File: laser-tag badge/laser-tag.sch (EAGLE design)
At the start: 32 parts, among them U1 MKL27Z256VLH4

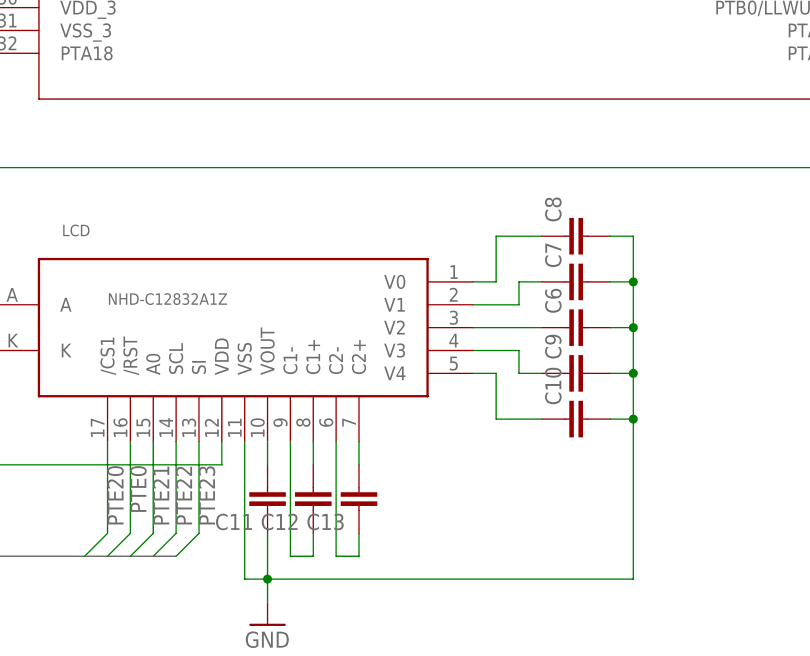
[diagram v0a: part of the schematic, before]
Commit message: Add LCD capacitor values
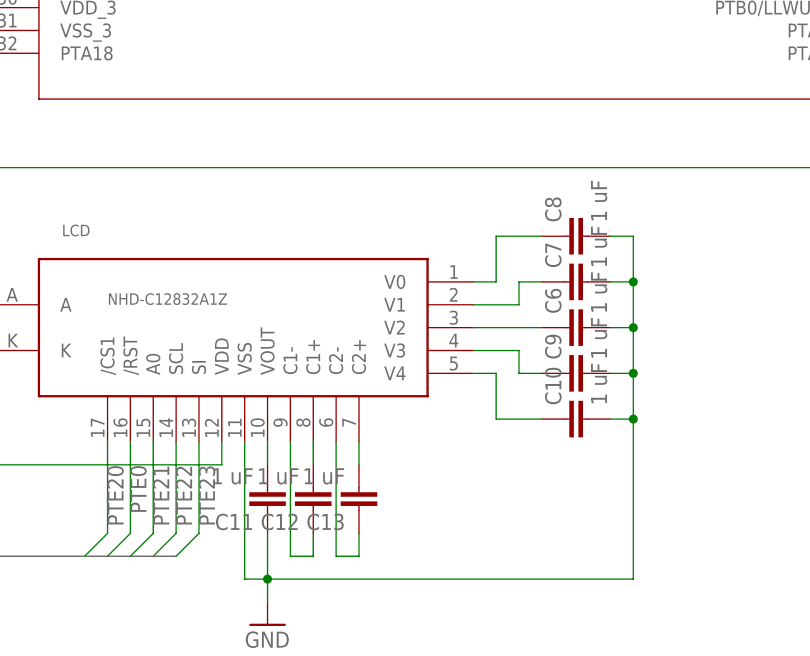
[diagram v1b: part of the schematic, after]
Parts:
- C10, C11, C12, C13, C6, C7, C8, C9: value (none) -> 1 uF
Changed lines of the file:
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@@
 <part name="P+5" library="supply1" deviceset="VCC" device=""/>
 <part name="LCD" library="Displays" deviceset="NHD-C12832A1Z" device=""/>
-<part name="C6" library="rcl" deviceset="C-EU" device="C0603K"/>
-<part name="C7" library="rcl" deviceset="C-EU" device="C0603K"/>
-<part name="C8" library="rcl" deviceset="C-EU" device="C0603K"/>
-<part name="C9" library="rcl" deviceset="C-EU" device="C0603K"/>
-<part name="C10" library="rcl" deviceset="C-EU" device="C0603K"/>
-<part name="C11" library="rcl" deviceset="C-EU" device="C0603K"/>
-<part name="C12" library="rcl" deviceset="C-EU" device="C0603K"/>
-<part name="C13" library="rcl" deviceset="C-EU" device="C0603K"/>
+<part name="C6" library="rcl" deviceset="C-EU" device="C0603K" value="1 uF"/>
+<part name="C7" library="rcl" deviceset="C-EU" device="C0603K" value="1 uF"/>
+<part name="C8" library="rcl" deviceset="C-EU" device="C0603K" value="1 uF"/>
+<part name="C9" library="rcl" deviceset="C-EU" device="C0603K" value="1 uF"/>
+<part name="C10" library="rcl" deviceset="C-EU" device="C0603K" value="1 uF"/>
+<part name="C11" library="rcl" deviceset="C-EU" device="C0603K" value="1 uF"/>
+<part name="C12" library="rcl" deviceset="C-EU" device="C0603K" value="1 uF"/>
+<part name="C13" library="rcl" deviceset="C-EU" device="C0603K" value="1 uF"/>
 <part name="GND6" library="supply1" deviceset="GND" device=""/>
 <part name="GND7" library="supply1" deviceset="GND" device=""/>

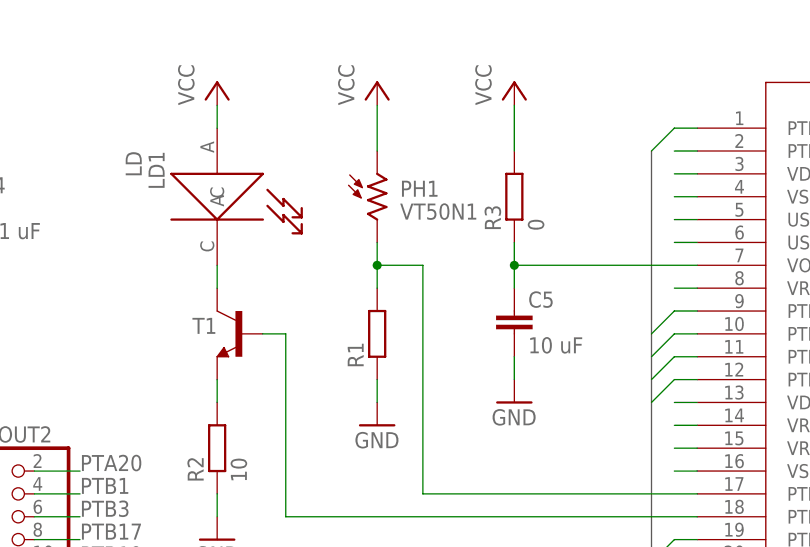
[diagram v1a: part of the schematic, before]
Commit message: Changed to photodiode and added pingpong placement
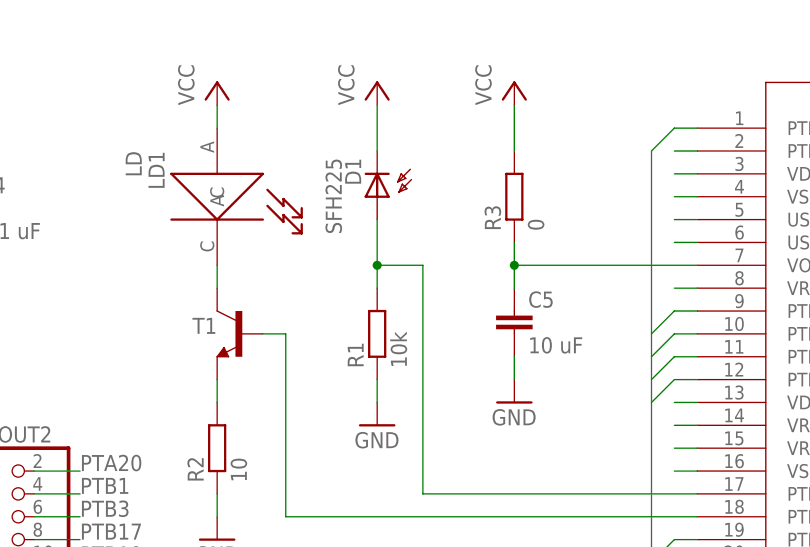
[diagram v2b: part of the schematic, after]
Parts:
- removed PH1: VT50N1, photo-elements:VT50N1
- added D1: SFH225, opto-trans-siemens:SFH225
- R1: value (none) -> 10k
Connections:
- net PTE29: now also D1.A; no longer PH1.2
- net VCC: now also D1.C; no longer PH1.1
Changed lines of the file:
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@@
 <part name="T1" library="transistor" deviceset="*-NPN-" device="SOT23-EBC"/>
 <part name="GND1" library="supply1" deviceset="GND" device=""/>
-<part name="PH1" library="photo-elements" deviceset="VT5*" device="" technology="0N1"/>
 <part name="P+2" library="supply1" deviceset="VCC" device=""/>
-<part name="R1" library="rcl" deviceset="R-EU_" device="R0603"/>
+<part name="R1" library="rcl" deviceset="R-EU_" device="R0603" value="10k"/>
 <part name="GND2" library="supply1" deviceset="GND" device=""/>
 <part name="USB" library="adafruit" deviceset="USB" device="MINIB"/>
@@
 <part name="S4" library="switch" deviceset="SKHMP*E010" device="" technology="S"/>
 <part name="GND8" library="supply1" deviceset="GND" device=""/>
+<part name="D1" library="opto-trans-siemens" deviceset="SFH225" device=""/>
 </parts>
 <sheets>
@@
 </instance>
 <instance part="GND1" gate="1" x="-43.18" y="53.34"/>
-<instance part="PH1" gate="G$1" x="-25.4" y="91.44"/>
 <instance part="P+2" gate="VCC" x="-25.4" y="104.14"/>
 <instance part="R1" gate="G$1" x="-25.4" y="76.2" rot="R90"/>
@@
 <instance part="S4" gate="G$1" x="147.32" y="73.66"/>
 <instance part="GND8" gate="1" x="157.48" y="17.78"/>
+<instance part="D1" gate="1" x="-25.4" y="91.44" rot="R180"/>
 </instances>
 <busses>
@@
 <segment>
 <pinref part="P+2" gate="VCC" pin="VCC"/>
-<pinref part="PH1" gate="G$1" pin="1"/>
 <wire x1="-25.4" y1="101.6" x2="-25.4" y2="96.52" width="0.1524" layer="91"/>
+<pinref part="D1" gate="1" pin="C"/>
 </segment>
 <segment>
@@
 </segment>
 <segment>
-<pinref part="PH1" gate="G$1" pin="2"/>
 <pinref part="R1" gate="G$1" pin="2"/>
-<wire x1="-25.4" y1="86.36" x2="-25.4" y2="83.82" width="0.1524" layer="91"/>
 <wire x1="-25.4" y1="83.82" x2="-25.4" y2="81.28" width="0.1524" layer="91"/>
 <wire x1="-25.4" y1="83.82" x2="-20.32" y2="83.82" width="0.1524" layer="91"/>
@@
 <wire x1="-20.32" y1="83.82" x2="-20.32" y2="58.42" width="0.1524" layer="91"/>
 <wire x1="-20.32" y1="58.42" x2="10.16" y2="58.42" width="0.1524" layer="91"/>
-</segment>
-</net>
+<pinref part="D1" gate="1" pin="A"/>
+<wire x1="-25.4" y1="88.9" x2="-25.4" y2="83.82" width="0.1524" layer="91"/>
+</segment>
+</net>

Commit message: New board design
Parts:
- added D2: PDB-C154SM, Photonics:PDB-C154SM
- D1: value SFH225 -> PDB-C154SM; device opto-trans-siemens:SFH225 -> Photonics:PDB-C154SM
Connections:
- net PTE29: now also D2.A
- net VCC: now also D2.C
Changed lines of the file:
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@@
 <layer number="56" name="wert" color="7" fill="1" visible="no" active="no"/>
 <layer number="57" name="tCAD" color="7" fill="1" visible="no" active="no"/>
+<layer number="59" name="tCarbon" color="7" fill="1" visible="no" active="no"/>
+<layer number="60" name="bCarbon" color="7" fill="1" visible="no" active="no"/>
 <layer number="90" name="Modules" color="7" fill="1" visible="no" active="yes"/>
 <layer number="91" name="Nets" color="2" fill="1" visible="yes" active="yes"/>
@@
 <layer number="127" name="_tValues" color="7" fill="1" visible="no" active="yes"/>
 <layer number="128" name="_bValues" color="7" fill="1" visible="no" active="yes"/>
+<layer number="129" name="Mask" color="7" fill="1" visible="yes" active="yes"/>
 <layer number="131" name="tAdjust" color="7" fill="1" visible="no" active="yes"/>
 <layer number="132" name="bAdjust" color="7" fill="1" visible="no" active="yes"/>
@@
 <layer number="223" name="223bmp" color="24" fill="1" visible="no" active="no"/>
 <layer number="224" name="224bmp" color="25" fill="1" visible="no" active="no"/>
+<layer number="225" name="225bmp" color="7" fill="1" visible="yes" active="yes"/>
+<layer number="226" name="226bmp" color="7" fill="1" visible="yes" active="yes"/>
+<layer number="227" name="227bmp" color="7" fill="1" visible="yes" active="yes"/>
+<layer number="228" name="228bmp" color="7" fill="1" visible="yes" active="yes"/>
+<layer number="229" name="229bmp" color="7" fill="1" visible="yes" active="yes"/>
+<layer number="230" name="230bmp" color="7" fill="1" visible="yes" active="yes"/>
 <layer number="231" name="Eagle3D_PG1" color="7" fill="1" visible="no" active="no"/>
 <layer number="232" name="Eagle3D_PG2" color="7" fill="1" visible="no" active="no"/>
@@
 <layer number="251" name="SMDround" color="7" fill="1" visible="no" active="no"/>
 <layer number="254" name="cooling" color="7" fill="1" visible="no" active="yes"/>
+<layer number="255" name="routoute" color="7" fill="1" visible="yes" active="yes"/>
 </layers>
 <schematic xreflabel="%F%N/%S.%C%R" xrefpart="/%S.%C%R">
@@
 <part name="S4" library="switch" deviceset="SKHMP*E010" device="" technology="S"/>
 <part name="GND8" library="supply1" deviceset="GND" device=""/>
-<part name="D1" library="opto-trans-siemens" deviceset="SFH225" device=""/>
+<part name="D1" library="Photonics" deviceset="PDB-C154SM" device=""/>
+<part name="D2" library="Photonics" deviceset="PDB-C154SM" device=""/>
 </parts>
 <sheets>
@@
 <instance part="S4" gate="G$1" x="147.32" y="73.66"/>
 <instance part="GND8" gate="1" x="157.48" y="17.78"/>
-<instance part="D1" gate="1" x="-25.4" y="91.44" rot="R180"/>
+<instance part="D1" gate="G$1" x="-25.4" y="91.44" smashed="yes" rot="R180">
+<attribute name="NAME" x="-24.638" y="95.504" size="1.778" layer="95"/>
+</instance>
+<instance part="D2" gate="G$1" x="-20.32" y="91.44" smashed="yes" rot="R180">
+<attribute name="NAME" x="-19.558" y="95.504" size="1.778" layer="95"/>
+</instance>
 </instances>
 <busses>
@@
 <segment>
 <pinref part="P+2" gate="VCC" pin="VCC"/>
-<wire x1="-25.4" y1="101.6" x2="-25.4" y2="96.52" width="0.1524" layer="91"/>
-<pinref part="D1" gate="1" pin="C"/>
+<wire x1="-25.4" y1="101.6" x2="-25.4" y2="99.06" width="0.1524" layer="91"/>
+<pinref part="D1" gate="G$1" pin="C"/>
+<pinref part="D2" gate="G$1" pin="C"/>
+<wire x1="-25.4" y1="99.06" x2="-25.4" y2="96.52" width="0.1524" layer="91"/>
+<wire x1="-20.32" y1="96.52" x2="-20.32" y2="99.06" width="0.1524" layer="91"/>
+<wire x1="-20.32" y1="99.06" x2="-25.4" y2="99.06" width="0.1524" layer="91"/>
+<junction x="-25.4" y="99.06"/>
 </segment>
 <segment>
@@
 <wire x1="-20.32" y1="83.82" x2="-20.32" y2="58.42" width="0.1524" layer="91"/>
 <wire x1="-20.32" y1="58.42" x2="10.16" y2="58.42" width="0.1524" layer="91"/>
-<pinref part="D1" gate="1" pin="A"/>
-<wire x1="-25.4" y1="88.9" x2="-25.4" y2="83.82" width="0.1524" layer="91"/>
-</segment>
-</net>
+<wire x1="-25.4" y1="88.9" x2="-25.4" y2="86.36" width="0.1524" layer="91"/>
+<pinref part="D1" gate="G$1" pin="A"/>
+<pinref part="D2" gate="G$1" pin="A"/>
+<wire x1="-25.4" y1="86.36" x2="-25.4" y2="83.82" width="0.1524" layer="91"/>
+<wire x1="-20.32" y1="88.9" x2="-20.32" y2="86.36" width="0.1524" layer="91"/>
+<wire x1="-20.32" y1="86.36" x2="-25.4" y2="86.36" width="0.1524" layer="91"/>
+<junction x="-25.4" y="86.36"/>
+</segment>
+</net>

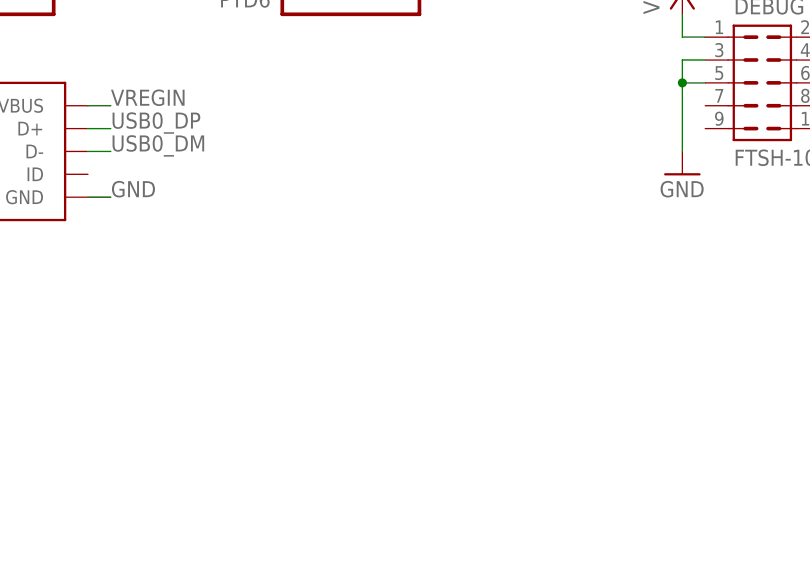
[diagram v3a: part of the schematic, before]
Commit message: Added AHA logo
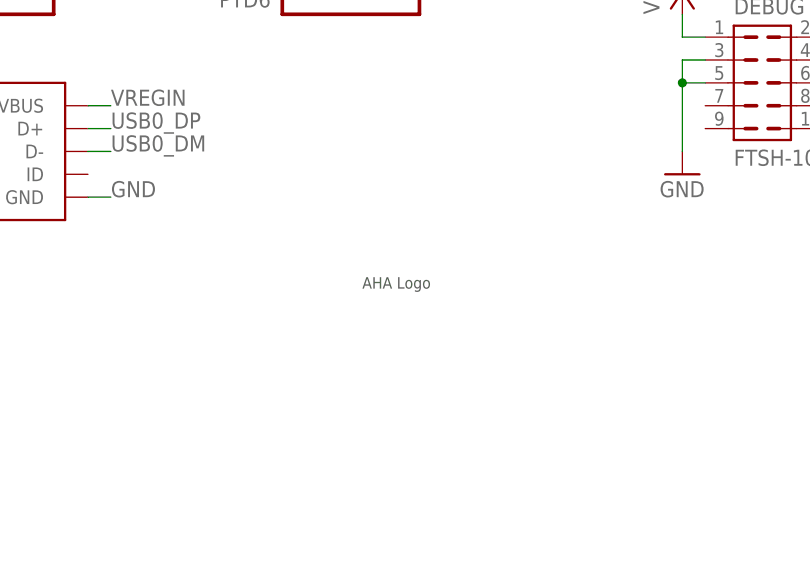
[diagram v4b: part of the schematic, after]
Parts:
- added U$1: AHA, Graphics:AHA
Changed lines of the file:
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@@
 <part name="D1" library="Photonics" deviceset="PDB-C154SM" device=""/>
 <part name="D2" library="Photonics" deviceset="PDB-C154SM" device=""/>
+<part name="U$1" library="Graphics" deviceset="AHA" device=""/>
 </parts>
 <sheets>
@@
 <attribute name="NAME" x="-19.558" y="95.504" size="1.778" layer="95"/>
 </instance>
+<instance part="U$1" gate="G$1" x="-66.04" y="-10.16"/>
 </instances>
 <busses>
